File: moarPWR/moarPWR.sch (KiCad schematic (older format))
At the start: 0 parts

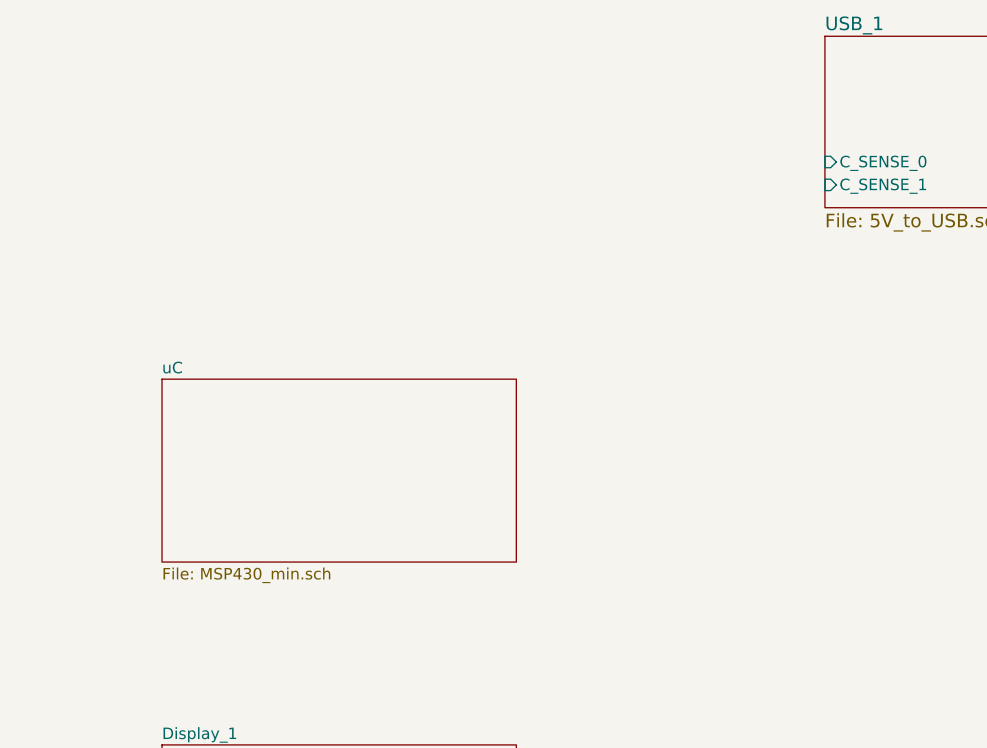
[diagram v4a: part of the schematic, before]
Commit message: Added I2C
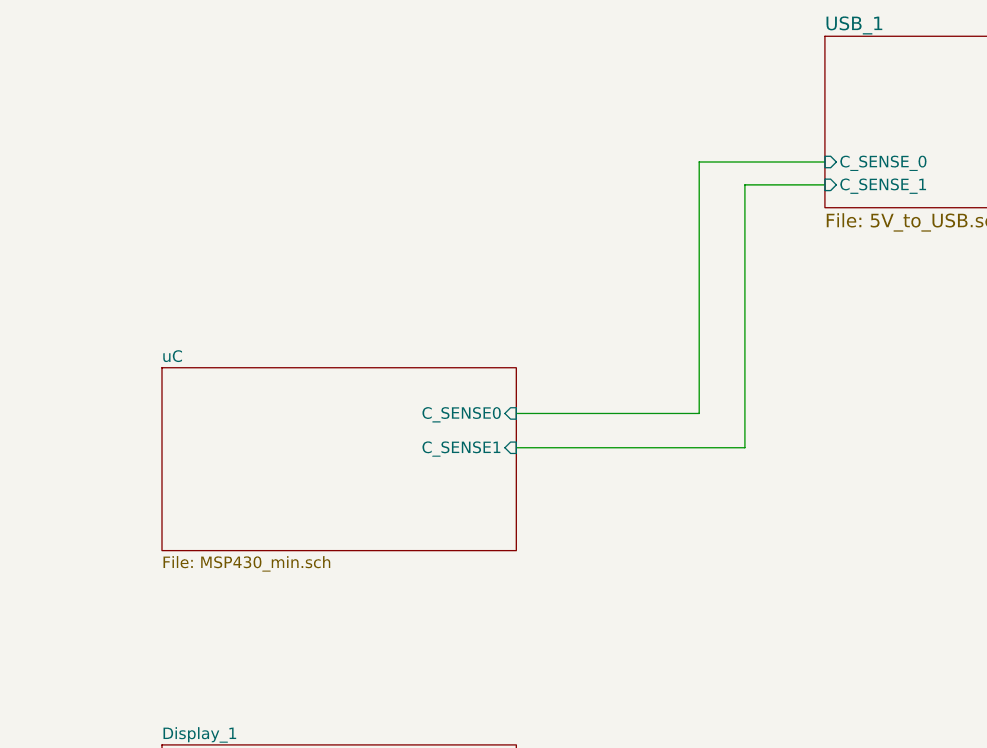
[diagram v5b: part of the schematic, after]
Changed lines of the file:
@@
 $EndSheet
 $Sheet
-S 4500 3750 1550 800
+S 4500 3700 1550 800
 U 5C623F3F
 F0 "uC" 50
 F1 "MSP430_min.sch" 50
+F2 "C_SENSE0" I R 6050 3900 50
+F3 "C_SENSE1" I R 6050 4050 50
 $EndSheet
+Wire Wire Line
+	7400 2800 6850 2800
+Wire Wire Line
+	6850 2800 6850 3900
+Wire Wire Line
+	6850 3900 6050 3900
+Wire Wire Line
+	6050 4050 7050 4050
+Wire Wire Line
+	7050 4050 7050 2900
+Wire Wire Line
+	7050 2900 7400 2900
 $EndSCHEMATC
